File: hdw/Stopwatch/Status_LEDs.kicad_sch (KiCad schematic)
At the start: 43 parts, among them U601 74LVC1G06, U602 74LVC1G06, U603 74LVC1G06, U604 74LVC1G06, U605 74LVC1G06, U606 74LVC1G06, U607 74LVC1G06, U608 74LVC1G06, U609 74LVC1G06

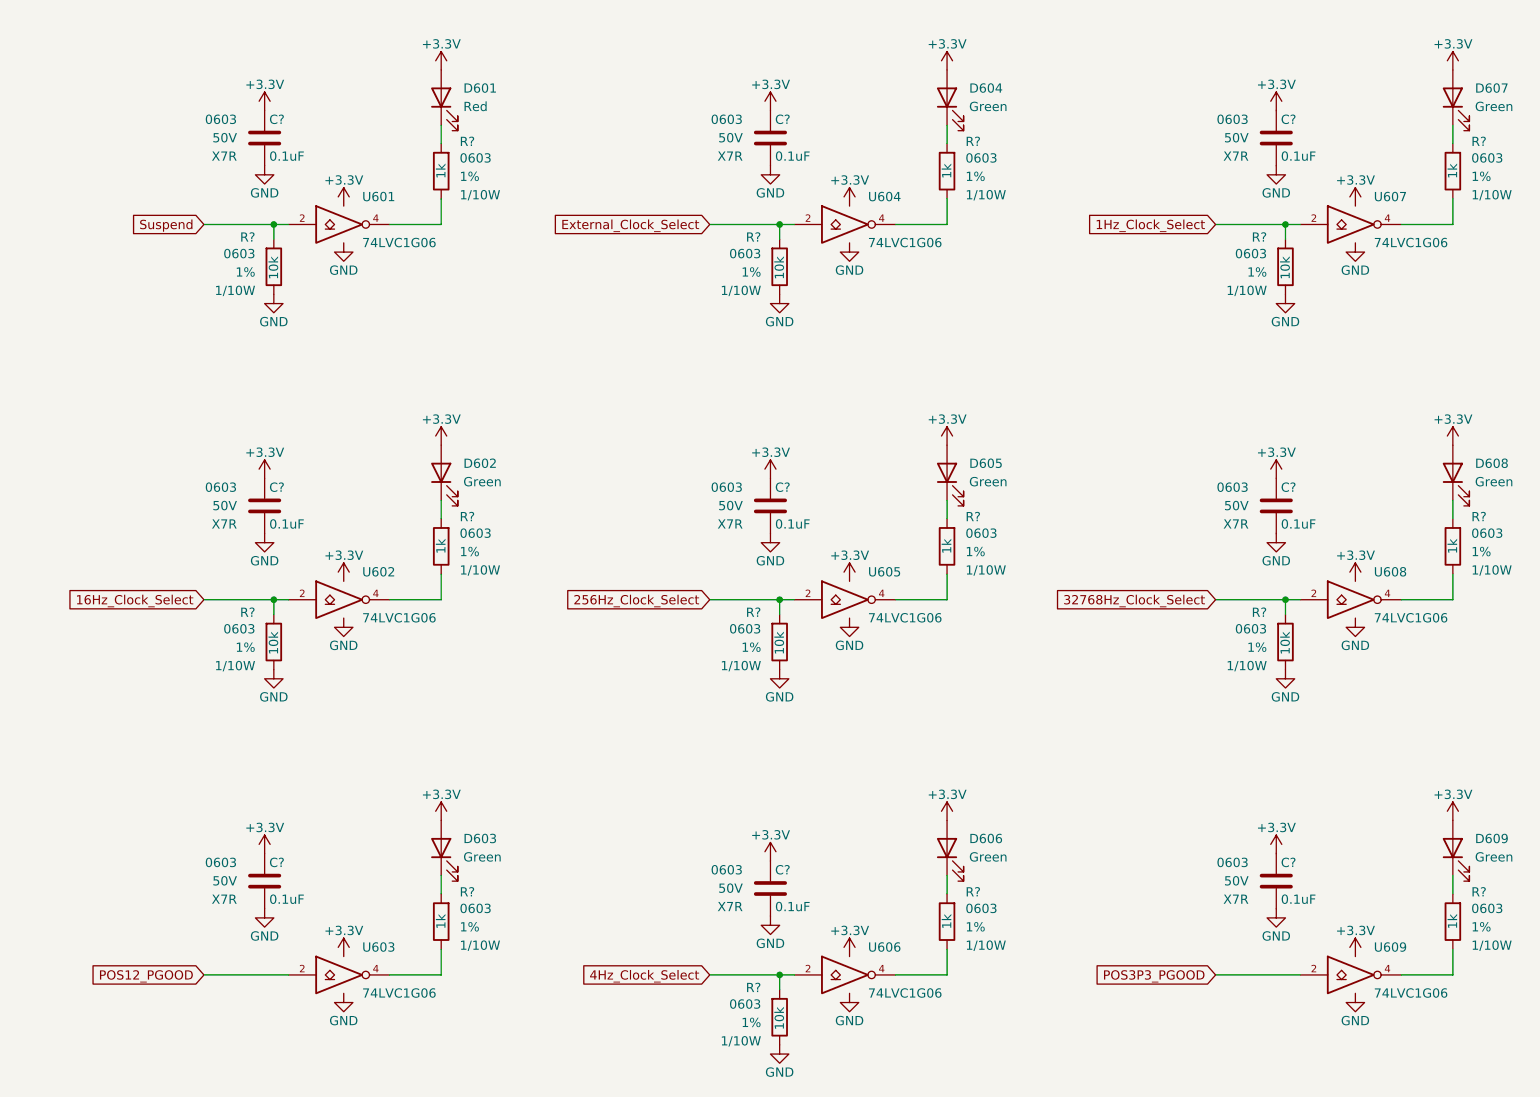
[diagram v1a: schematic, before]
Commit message: adjusted stage sheet
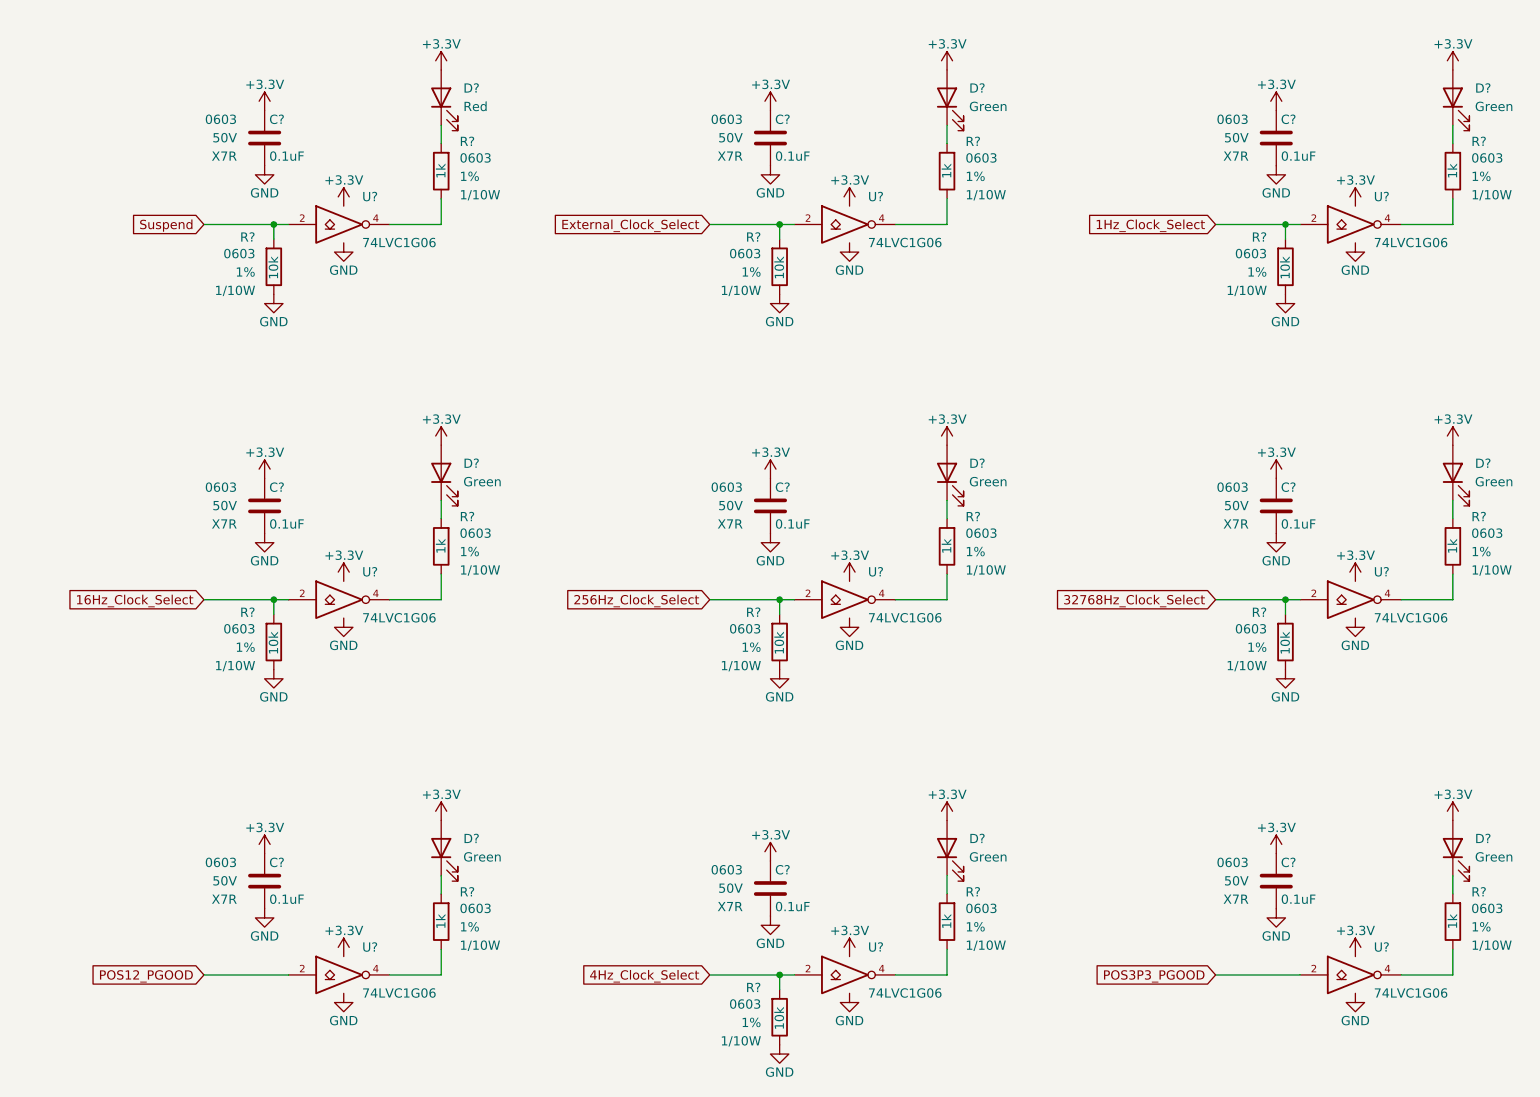
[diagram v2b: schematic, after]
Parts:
- renumbered D603 to D?, D601 to D?, D604 to D?, D607 to D?, D606 to D?, D602 to D?, D605 to D?, D608 to D?, D609 to D?, U603 to U?, U601 to U?, U604 to U?, U607 to U?, U606 to U?, U602 to U?, U605 to U?, U608 to U?, U609 to U?

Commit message: added reset stuff
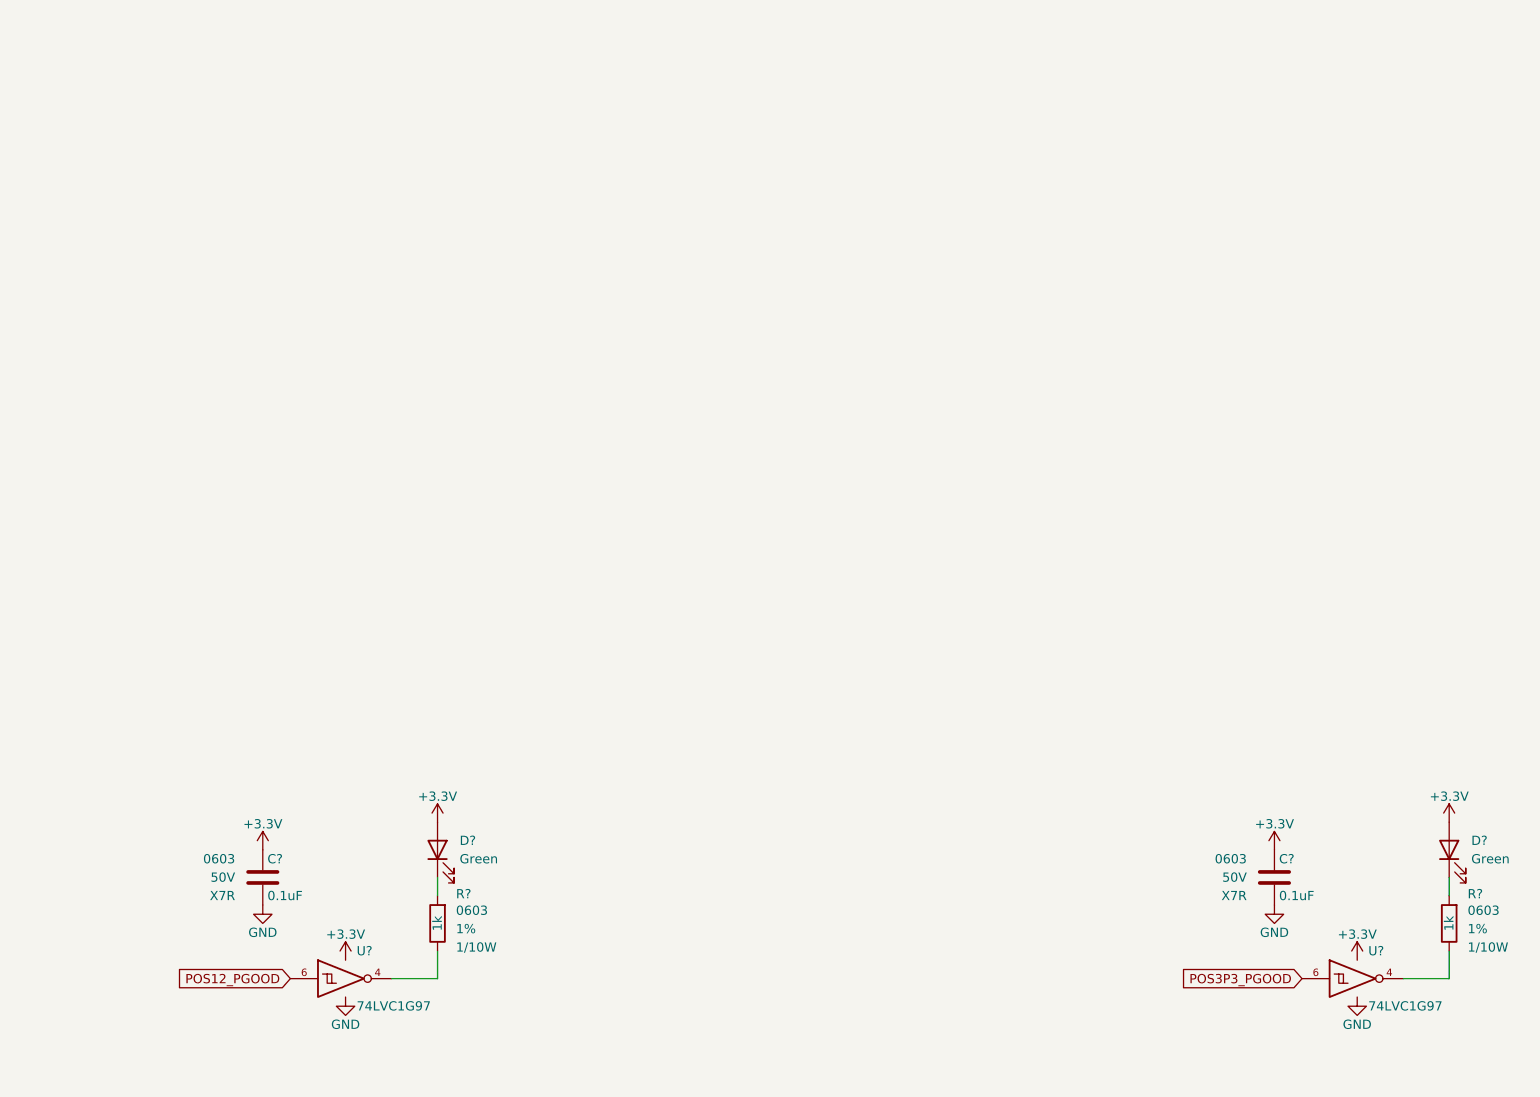
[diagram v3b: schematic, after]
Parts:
- removed C? (x7): 0.1uF, Capacitors_SMD:C_0603, symbol Custom_Library:C_Custom
- removed D?: Red, LEDs:LED_0603, symbol Device:LED
- removed D? (x6): Green, LEDs:LED_0603, symbol Device:LED
- removed R? (x7): 10k, Resistors_SMD:R_0603, symbol Custom_Library:R_Custom
- removed R? (x7): 1k, Resistors_SMD:R_0603, symbol Custom_Library:R_Custom
- removed U? (x9): 74LVC1G06, TO_SOT_Packages_SMD:SOT-353_SC-70-5, symbol Custom_Library:74LVC1G06_Power
- added U? (x2): 74LVC1G97, Package_TO_SOT_SMD:SOT-363_SC-70-6, symbol Custom Library:74LVC1G97_Power_NOT
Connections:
- net +3V3: now also U?.1 (VCC), U?.1 (VCC), U?.5 (VCC), U?.5 (VCC)
- net GND: now also U?.2 (GND), U?.2 (GND), U?.3 (GND), U?.3 (GND)
- net POS12_PGOOD: now also U?.6
- net POS3P3_PGOOD: now also U?.6
- net at R?.2: now also U?.4 (x2)
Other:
- moved on the sheet: C?, D?, R?

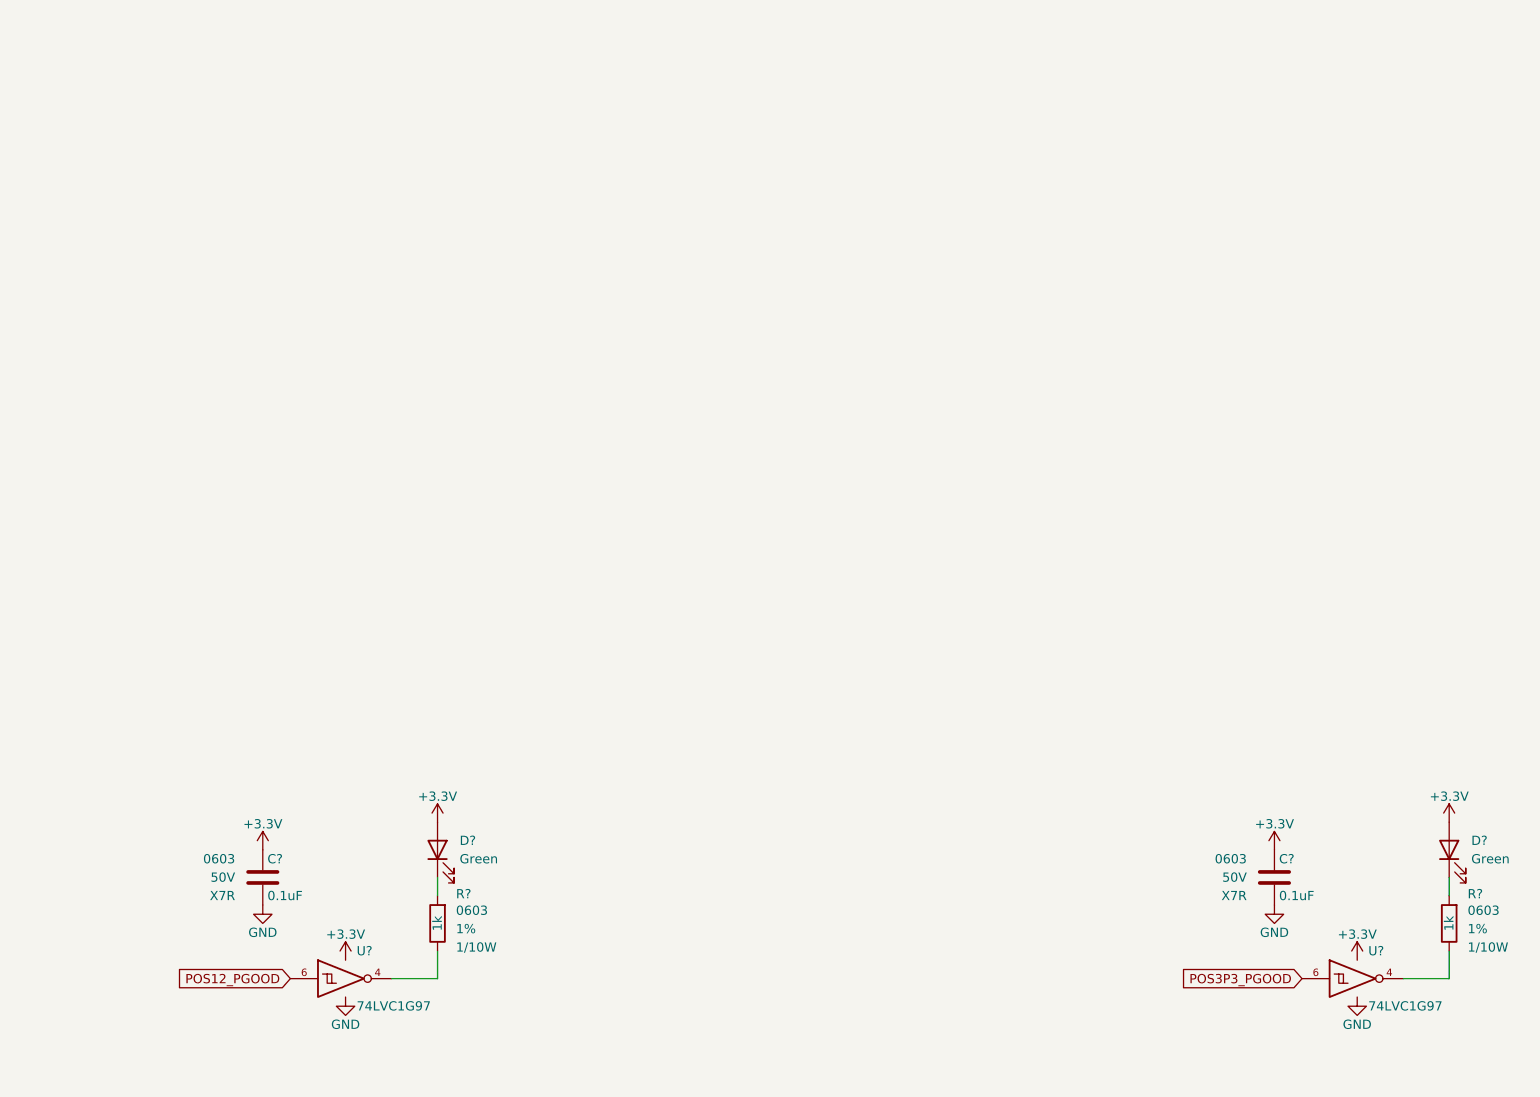
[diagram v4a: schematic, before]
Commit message: reordered schematic sheets
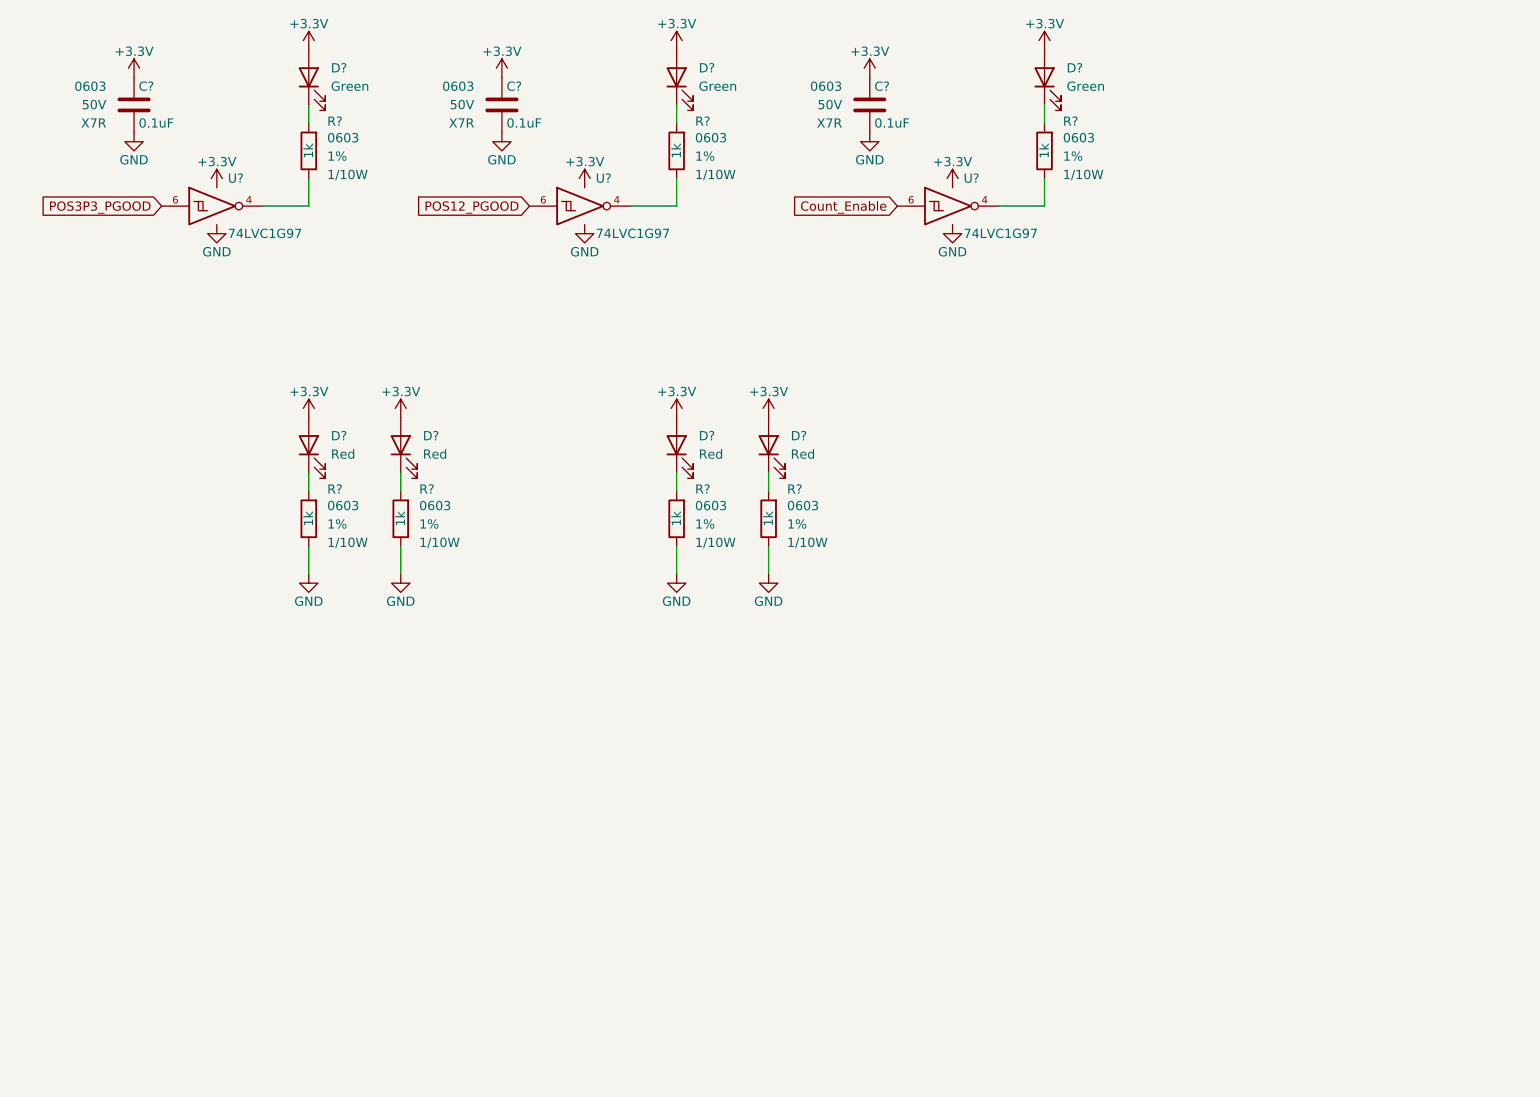
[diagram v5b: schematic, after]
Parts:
- added C?: 0.1uF, Capacitors_SMD:C_0603, symbol Custom_Library:C_Custom
- added D? (x4): Red, LEDs:LED_0603, symbol Device:LED
- added D?: Green, LEDs:LED_0603, symbol Device:LED
- added R? (x5): 1k, Resistors_SMD:R_0603, symbol Custom_Library:R_Custom
- added U?: 74LVC1G97, Package_TO_SOT_SMD:SOT-363_SC-70-6, symbol Custom Library:74LVC1G97_Power_NOT
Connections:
- net +3V3: now also C?.1, D?.2 (A), D?.2 (A), D?.2 (A), D?.2 (A), D?.2 (A), U?.1 (VCC), U?.5 (VCC)
- net GND: now also C?.2, R?.2, R?.2, R?.2, R?.2, U?.2 (GND), U?.3 (GND)
- new net: D?.1 (K), R?.1 (x5)
- new net: R?.2, U?.4
- new net Count_Enable: U?.6
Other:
- moved on the sheet: C?, D?, R?, U?
